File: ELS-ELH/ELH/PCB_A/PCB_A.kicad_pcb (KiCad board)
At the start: 2 copper layers, 95 x 95 mm, 44 parts, among them J1 PWR 1, J10 CH C OUT, J11 CH A OUT, J12 CH B OUT, J2 PWR 2, J3 PWR 3, J4 PWR 4, J5 PWR 2 OUT, J6 Conn_01x20_Pin, J7 Conn_01x20_Pin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

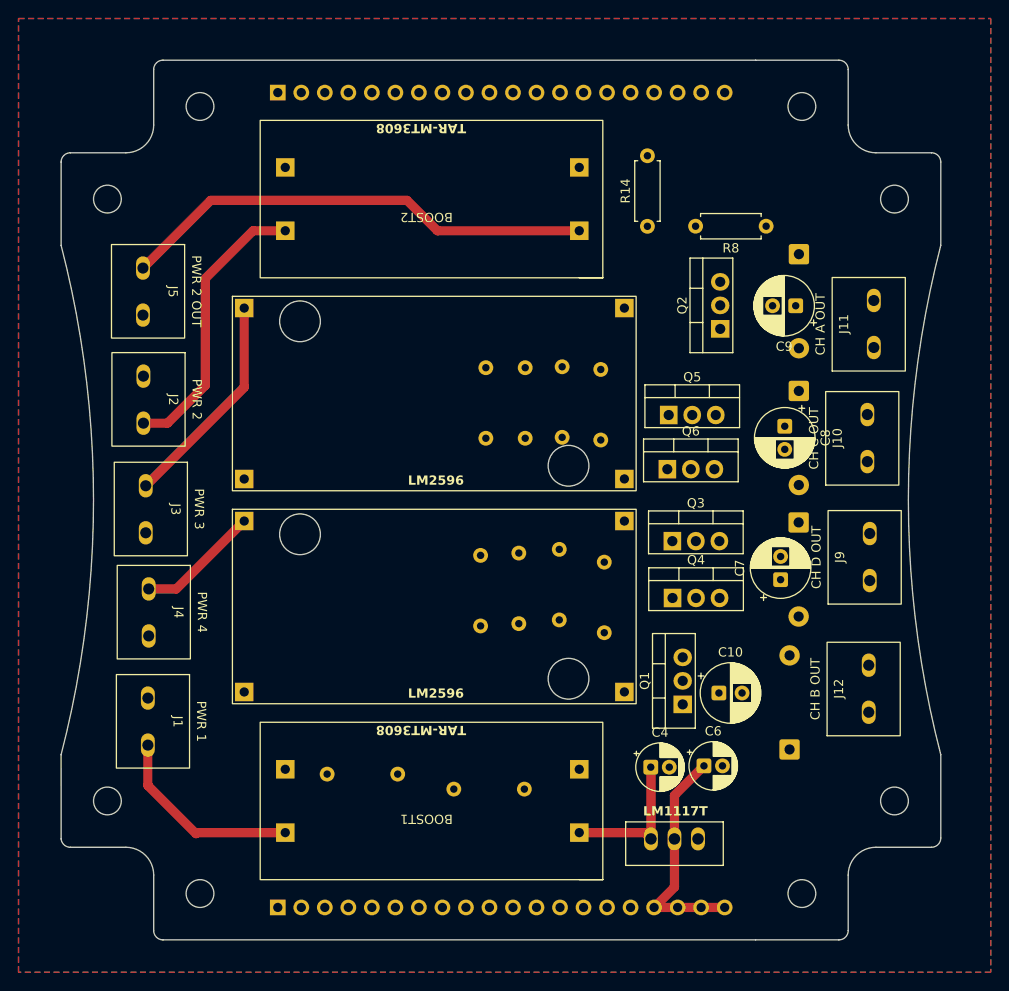
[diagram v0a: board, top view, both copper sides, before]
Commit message: PCB A routed
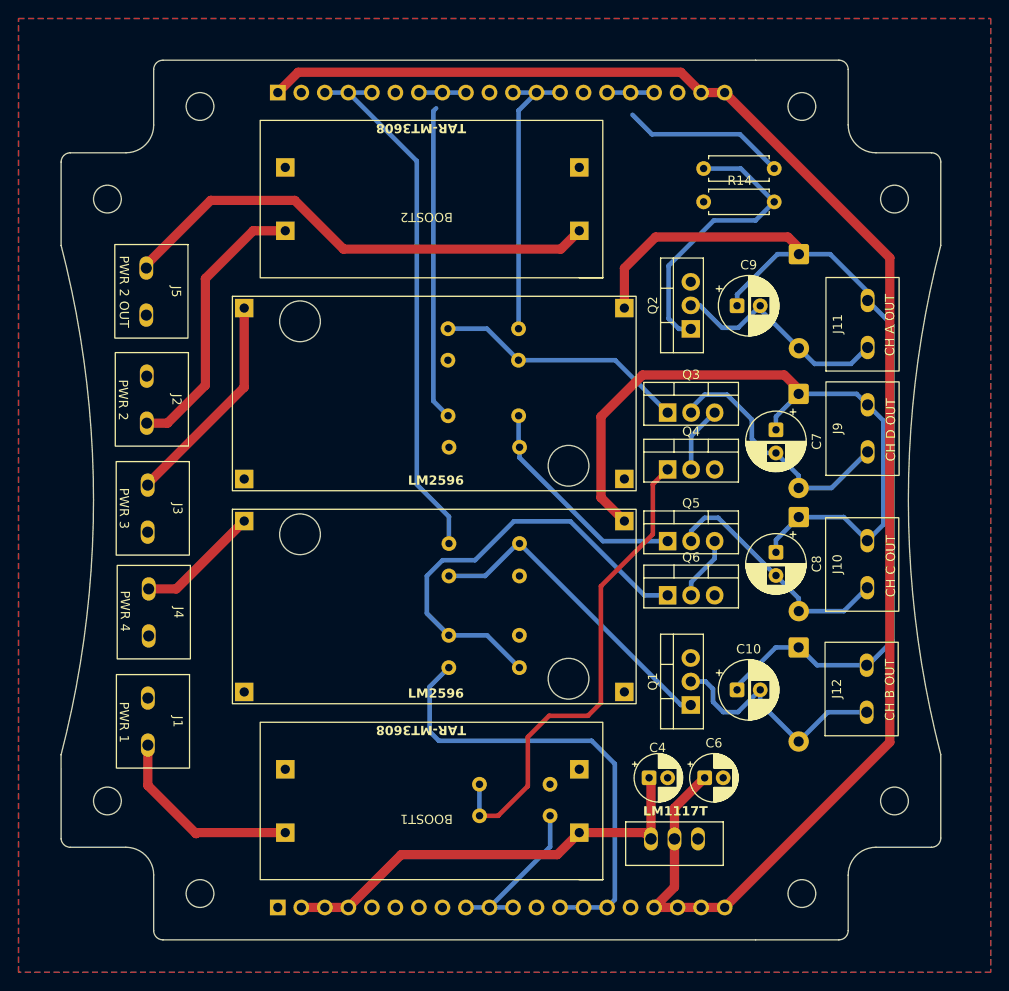
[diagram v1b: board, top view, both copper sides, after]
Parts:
- moved R10 33.4 mm to (-5.63, 18.1), turned to 0 degrees
- moved R11 31.9 mm to (1.90, -18.5), turned to 180 degrees
- moved R18 31.5 mm to (-5.63, 14.6), turned to 0 degrees
- moved R7 27.7 mm to (-5.62, 4.70), turned to 0 degrees
- moved R13 22.1 mm to (-5.62, 8.20), turned to 0 degrees
- moved R9 21.8 mm to (5.31, 34.1), turned to 180 degrees
- moved R16 21.2 mm to (-2.32, 30.7), turned to 0 degrees
- moved R15 20.9 mm to (1.89, -15.1), turned to 180 degrees
- moved C7 16.2 mm to (29.7, -7.58), turned to -90 degrees
- moved R14 13.9 mm to (29.5, -32.2), turned to 180 degrees
- moved J9 13.9 mm to (35.1, -2.66)
- moved Q4 13.9 mm to (18.0, -3.30)
- moved Q3 13.9 mm to (18.0, -9.44)
- moved D2 13.9 mm to (32.1, -11.5)
- moved C8 13.7 mm to (29.7, 5.65)
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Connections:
- R7 pad 1: /CH_B_MOSFET_ESP2_3V3 -> /CH_B_MOSFET_ESP_CTR_3V3
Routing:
- net +3.3V_SENSORS: track 25.1 -> 176.7 mm
- net PWR 3 REG: track 0.00 -> 104.1 mm
- net PWR 4 REG: track 0.00 -> 78.9 mm
- net /CH_B_MOSFET_ESP_CTR_3V3: track 0.00 -> 58.3 mm
- net Net-(Q4-G): track 0.00 -> 52.9 mm
- net /CH_C_MOSFET_ESP_MAIN_3V3: track 0.00 -> 50.1 mm
- net Net-(Q6-G): track 0.00 -> 48.2 mm
- net /CH_C_MOSFET_ESP_CTR_3V3: track 0.00 -> 39.1 mm
- net Net-(Q1-G): track 0.00 -> 34.6 mm
- net +5V_MCU: track 15.8 -> 48.1 mm
- net Net-(Q2-G): track 0.00 -> 31.9 mm
- net /CH_D_MOSFET_ESP_CTR_3V3: track 0.00 -> 31.4 mm
- net Net-(D2-A): track 0.00 -> 27.9 mm
- net Net-(Q3-G): track 0.00 -> 27.5 mm
- net Net-(D3-A): track 0.00 -> 26.7 mm
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
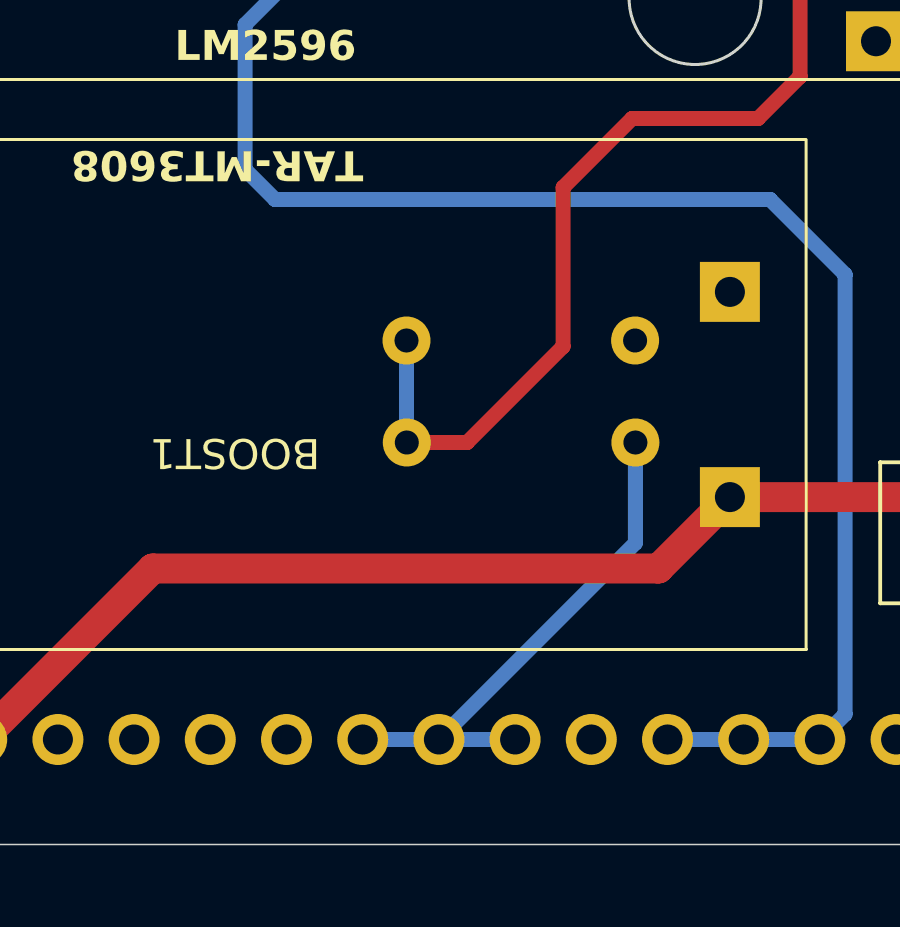
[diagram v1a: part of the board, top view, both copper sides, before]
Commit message: reorganized resistances
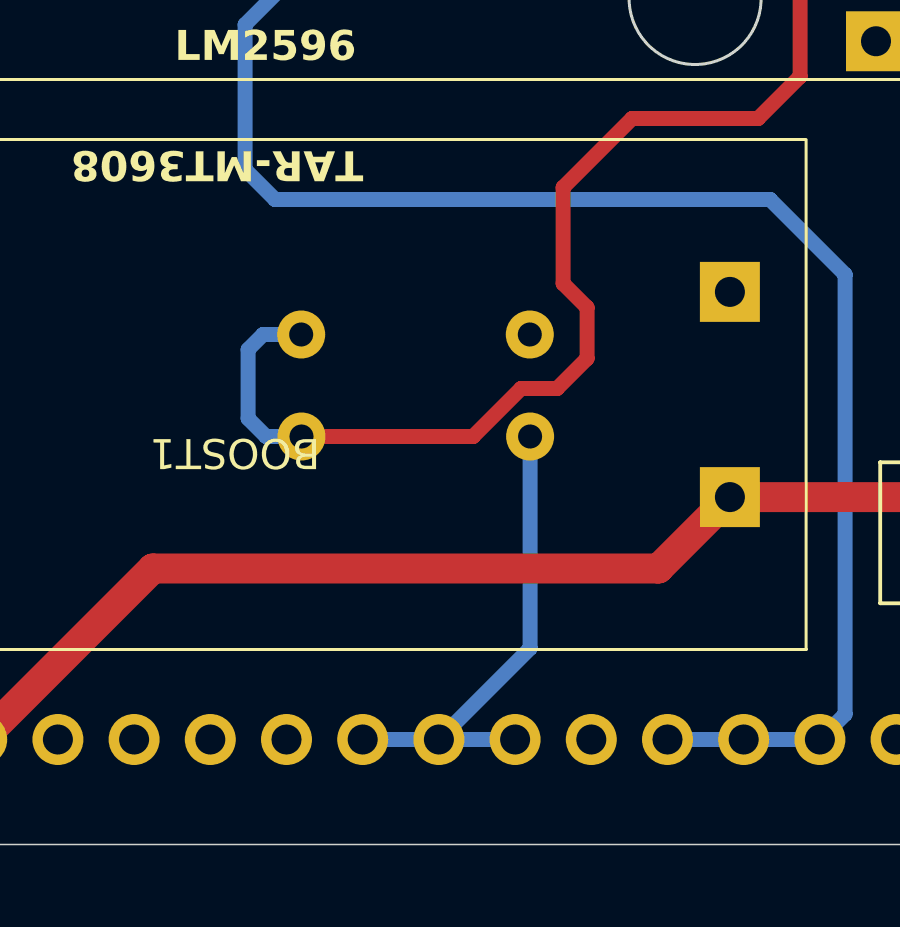
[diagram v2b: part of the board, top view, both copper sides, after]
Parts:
- moved R16 3.52 mm to (-5.83, 30.5)
- moved R9 3.52 mm to (1.80, 33.9)
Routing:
- net Net-(Q4-G): track 52.9 -> 60.5 mm
- net /CH_D_MOSFET_ESP_MAIN_3V3: track 17.7 -> 16.4 mm
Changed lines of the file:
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@@
 	(footprint "Resistor_THT:R_Axial_DIN0207_L6.3mm_D2.5mm_P7.62mm_Horizontal"
 		(layer "B.Cu")
-		(at -2.32 30.7)
+		(at -5.83 30.5)
 		(descr "Resistor, Axial_DIN0207 series, Axial, Horizontal, pin pitch=7.62mm, 0.25W = 1/4W, length*diameter=6.3*2.5mm^2, http://cdn-reichelt.de/documents/datenblatt/B400/1_4W%23YAG.pdf")
 		(tags "Resistor Axial_DIN0207 series Axial Horizontal pin pitch 7.62mm 0.25W = 1/4W length 6.3mm diameter 2.5mm")
@@
 	(footprint "Resistor_THT:R_Axial_DIN0207_L6.3mm_D2.5mm_P7.62mm_Horizontal"
 		(layer "B.Cu")
-		(at 5.31 34.1 180)
+		(at 1.8 33.9 180)
 		(descr "Resistor, Axial_DIN0207 series, Axial, Horizontal, pin pitch=7.62mm, 0.25W = 1/4W, length*diameter=6.3*2.5mm^2, http://cdn-reichelt.de/documents/datenblatt/B400/1_4W%23YAG.pdf")
 		(tags "Resistor Axial_DIN0207 series Axial Horizontal pin pitch 7.62mm 0.25W = 1/4W length 6.3mm diameter 2.5mm")
@@
 	)
 	(segment
-		(start 16.4 3.7)
-		(end 16.4 -1.7)
+		(start 9.4 23.3)
+		(end 10.8 21.9)
 		(width 0.5)
 		(layer "F.Cu")
@@
 	)
 	(segment
-		(start 16.4 -1.7)
-		(end 18 -3.3)
+		(start 2.9 28.8)
+		(end 2.9 25.6)
 		(width 0.5)
 		(layer "F.Cu")
@@
 	)
 	(segment
-		(start 9.4 23.3)
-		(end 10.8 21.9)
+		(start 2.700001 32.3)
+		(end 3.7 31.300001)
+		(width 0.5)
+		(layer "F.Cu")
+		(net "Net-(Q4-G)")
+	)
+	(segment
+		(start 1.5 32.3)
+		(end 2.700001 32.3)
 		(width 0.5)
 		(layer "F.Cu")
@@
 	)
 	(segment
-		(start -2.31 34.1)
-		(end -0.3 34.1)
+		(start 3.7 29.6)
+		(end 2.9 28.8)
 		(width 0.5)
 		(layer "F.Cu")
@@
 	)
 	(segment
-		(start 5.2 23.3)
-		(end 9.4 23.3)
+		(start 10.8 21.9)
+		(end 10.8 9.3)
+		(width 0.5)
+		(layer "F.Cu")
+		(net "Net-(Q4-G)")
+	)
+	(segment
+		(start 16.4 3.7)
+		(end 16.4 -1.7)
+		(width 0.5)
+		(layer "F.Cu")
+		(net "Net-(Q4-G)")
+	)
+	(segment
+		(start 3.7 31.300001)
+		(end 3.7 29.6)
 		(width 0.5)
 		(layer "F.Cu")
@@
 	)
 	(segment
-		(start -0.3 34.1)
-		(end 2.9 30.9)
+		(start -0.1 33.9)
+		(end 1.5 32.3)
 		(width 0.5)
 		(layer "F.Cu")
@@
 	)
 	(segment
-		(start 2.9 30.9)
-		(end 2.9 25.6)
+		(start 16.4 -1.7)
+		(end 18 -3.3)
 		(width 0.5)
 		(layer "F.Cu")
@@
 	)
 	(segment
-		(start 10.8 21.9)
-		(end 10.8 9.3)
+		(start -5.82 33.9)
+		(end -0.1 33.9)
+		(width 0.5)
+		(layer "F.Cu")
+		(net "Net-(Q4-G)")
+	)
+	(segment
+		(start 5.2 23.3)
+		(end 9.4 23.3)
 		(width 0.5)
 		(layer "F.Cu")
@@
 	)
 	(segment
-		(start -2.32 30.7)
-		(end -2.32 34.09)
+		(start -5.83 30.5)
+		(end -7.1 30.5)
+		(width 0.5)
+		(layer "B.Cu")
+		(net "Net-(Q4-G)")
+	)
+	(segment
+		(start -7.6 31)
+		(end -7.6 33.3)
 		(width 0.5)
 		(layer "B.Cu")
@@
 	)
 	(segment
-		(start -2.32 34.09)
-		(end -2.31 34.1)
+		(start -7.1 30.5)
+		(end -7.6 31)
+		(width 0.5)
+		(layer "B.Cu")
+		(net "Net-(Q4-G)")
+	)
+	(segment
+		(start -7 33.9)
+		(end -5.82 33.9)
+		(width 0.5)
+		(layer "B.Cu")
+		(net "Net-(Q4-G)")
+	)
+	(segment
+		(start -7.6 33.3)
+		(end -7 33.9)
 		(width 0.5)
 		(layer "B.Cu")
@@
 	)
 	(segment
-		(start 5.31 34.1)
-		(end 5.31 37.45)
+		(start -3.78 44)
+		(end -1.24 44)
 		(width 0.5)
 		(layer "B.Cu")
@@
 	)
 	(segment
-		(start 5.31 37.45)
+		(start 1.3 44)
 		(end -1.24 44)
 		(width 0.5)
@@
 	)
 	(segment
-		(start -3.78 44)
-		(end -1.24 44)
+		(start 1.8 33.9)
+		(end 1.8 40.96)
 		(width 0.5)
 		(layer "B.Cu")
@@
 	)
 	(segment
-		(start 1.3 44)
+		(start 1.8 40.96)
 		(end -1.24 44)
 		(width 0.5)

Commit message: regulator's names changed
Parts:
- Regulator1, Regulator2: value MP1584 -> LM2596
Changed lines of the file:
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@@
 			)
 		)
-		(property "Value" "MP1584"
+		(property "Value" "LM2596"
 			(at 21.36 5.8 0)
 			(unlocked yes)
@@
 			)
 		)
-		(property "Value" "MP1584"
+		(property "Value" "LM2596"
 			(at 21.36 5.8 0)
 			(unlocked yes)

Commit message: Update almost finished
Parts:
- C10, C7, C8, C9: value C_Polarized_Small -> 47uF
- C4, C6: value C_Polarized_Small -> 10uF
- J1: value PWR 1 -> PWR 1 IN
- J10: value CH C OUT -> - CH C OUT +
- J11: value CH A OUT -> - CH A OUT +
- J12: value CH B OUT -> - CH B OUT +
- J2: value PWR 2 -> PWR 2 IN
- J3: value PWR 3 -> PWR 3 IN
- J4: value PWR 4 -> PWR 4 IN
- J9: value CH D OUT -> - CH D OUT +
- R10, R11, R12, R7, R8: value R_US -> 220
- R13, R14, R15, R16, R17, R18: value R_US -> 10K
- moved C9 4.47 mm to (29.7, -22.5), turned to -90 degrees
- moved C10 4.25 mm to (29.7, 19.9), turned to -90 degrees
- moved D2 2.46 mm to (29.8, -12.0)
- moved D4 2.43 mm to (29.8, -26.7)
- moved D3 2.42 mm to (29.8, 2.00)
- moved D5 2.40 mm to (29.8, 15.9)
- moved J12 1.46 mm to (35.0, 24.0)
- moved Regulator3 1.31 mm to (20.1, 36.6)
- moved Q4 1.10 mm to (18.0, -2.20)
- moved J5 0.80 mm to (-33.0, -27.6)
- moved J2 0.75 mm to (-33.0, -15.9)
- moved Q6 0.71 mm to (18.0, 11.0)
- moved J9 0.66 mm to (35.1, -2.00)
- moved J3 0.65 mm to (-33.0, -4.15)
- moved J1 0.63 mm to (-33.0, 18.9)
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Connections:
- J7 pad 15: /CH_C_MOSFET_ESP_CTR_3V3 -> /CH_A_MOSFET_ESP_CTR_3V3
- J7 pad 16: /CH_C_MOSFET_ESP_CTR_3V3 -> /CH_A_MOSFET_ESP_CTR_3V3
- J7 pad 17: /CH_C_MOSFET_ESP_CTR_3V3 -> /CH_A_MOSFET_ESP_CTR_3V3
- J7 pad 7: /CH_A_MOSFET_ESP_CTR_3V3 -> /CH_C_MOSFET_ESP_CTR_3V3
- J7 pad 8: /CH_A_MOSFET_ESP_CTR_3V3 -> /CH_C_MOSFET_ESP_CTR_3V3
- J7 pad 9: /CH_A_MOSFET_ESP_CTR_3V3 -> /CH_C_MOSFET_ESP_CTR_3V3
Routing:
- net PWR 3 REG: track 104.1 -> 194.1 mm
- net Net-(Q4-G): track 60.5 -> 51.6 mm
- net /CH_C_MOSFET_ESP_MAIN_3V3: track 50.1 -> 45.0 mm
- net Net-(D3-A): track 26.7 -> 31.4 mm
- net Net-(D4-A): track 24.7 -> 28.5 mm
- net +5V_MCU: track 48.1 -> 50.6 mm
- net /CH_A_MOSFET_ESP_CTR_3V3: track 22.8 -> 25.3 mm
- net Net-(Q5-G): track 24.2 -> 26.3 mm
- net /CH_C_MOSFET_ESP_CTR_3V3: track 39.1 -> 41.0 mm
- net Net-(Q3-S): track 7.19 -> 8.29 mm
- net PWR 4 REG: track 78.9 -> 79.8 mm
- net Net-(Q1-G): track 34.6 -> 35.3 mm
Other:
- board text added: "+"
- board text added: "-"
- board text added: "D"
- board text added: "G"
- board text added: "GND"
- board text added: "IN"
- board text added: "OUT"
- board text added: "S"

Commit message: Finished the manufacture
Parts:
- added G***: LOGO, ELH_Library:deltav_logo, F.Cu at (34.2, 28.6)
- added G***: LOGO, ELH_Library:volta_logo, F.Cu at (29.7, 31.8)
- added G***: LOGO, ELH_Library:IREC, F.Cu at (35.0, 34.9)
- added G***: LOGO, ELH_Library:colombia_aguila, B.Cu at (-7.30, -30.5)
- added G***: LOGO, ELH_Library:junior, B.Cu at (-28.7, -31.7)
- added G***: LOGO, ELH_Library:firmes_por_aero, B.Cu at (-17.1, 17.6)
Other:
- board text added: "3V3"
- board text added: "5V"
- board text added: "CH A CTR"
- board text added: "CH B CTR"
- board text added: "CH C CTR"
- board text added: "CH C MAIN"
- board text added: "CH D CTR"
- board text added: "CH D MAIN"
- board text added: "JUNIOR TU PAPÁ LOS DEMÁS VALEN *****"
- board text added: "🎶 AMARTE MÁS NO PUDE 🎶"
